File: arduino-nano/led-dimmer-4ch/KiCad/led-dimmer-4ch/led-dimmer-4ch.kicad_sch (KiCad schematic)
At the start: 32 parts, among them J1 Screw_Terminal_01x02, J2 Screw_Terminal_01x08, U1 LM2596S-5

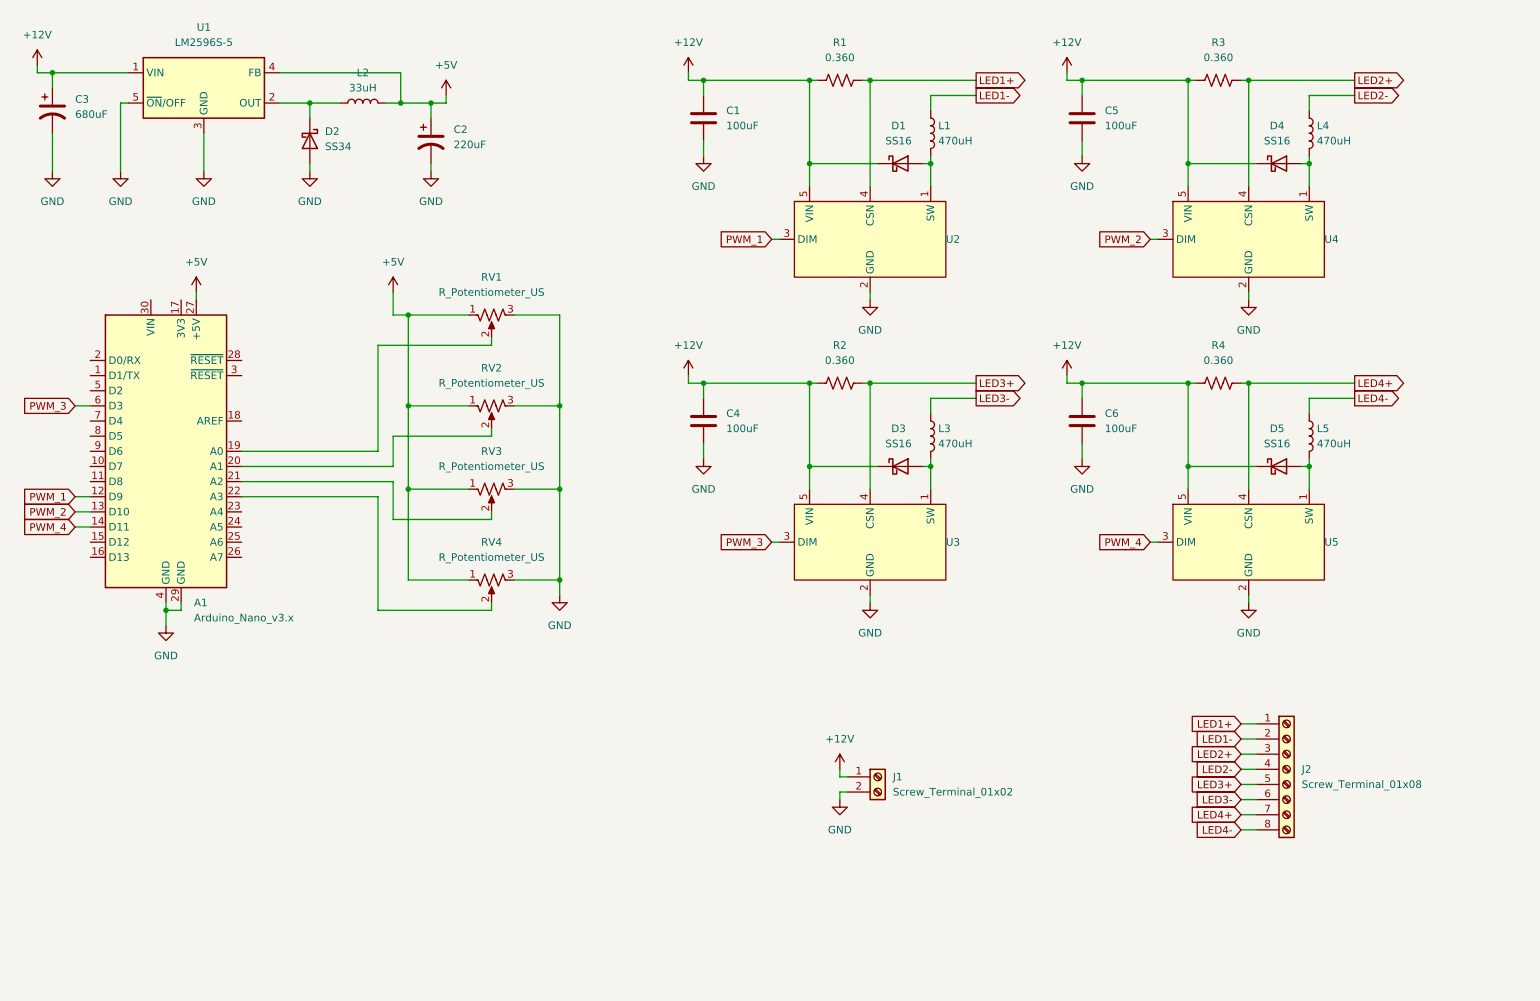
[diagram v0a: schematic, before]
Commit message: feat(led-dimmer-4ch): move pots off-board, swap to the AP63205 buck, and lay out the board
- What: RV1-RV4 become J4/J5 terminals with 100nF ADC caps, LED outputs split across J2/J3, DIM pins get 10k pull-downs, the LM2596 block becomes the microwave's AP63205 layout, and the PCB is placed with identical channel blocks, corner M3 holes, and GND/+12V pours.
- Why: pots now live on a separate panel board, DIM floated high through the PT4115's internal pull-up at reset, the inductors and input caps were outside the datasheet's ranges, and the layout had no outline.
- How: 4-pin 5.00 mm terminals, one 25 mil grid channel template repeated at 500 mil pitch, and the buck block copied from the microwave with nets remapped pad by pad and mirrored to F.Cu.
- Benefit: LEDs stay off through reset, the buck is shared and proven across both boards, and the board shrinks to 3.1 x 2.6 in with USB on the edge.
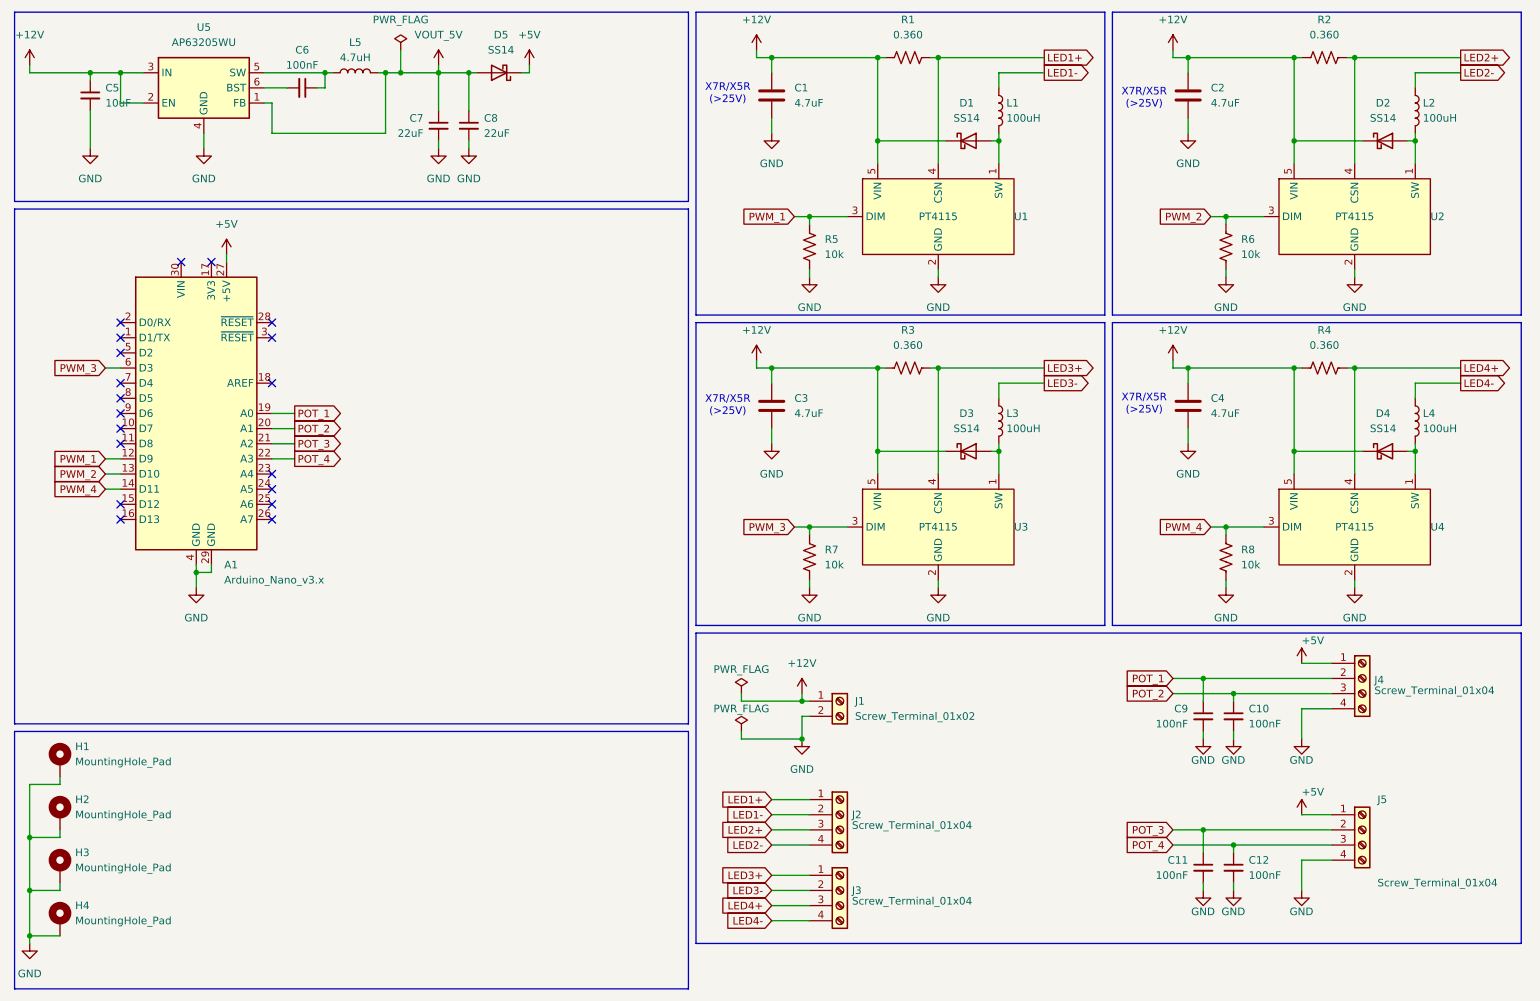
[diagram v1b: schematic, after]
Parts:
- removed C2: 220uF, symbol Device:C_Polarized_US
- removed C3: 680uF, symbol Device:C_Polarized_US
- removed D1, D3, D4, D5: SS16, Diode_SMD:D_SMA, symbol Diode:SS16
- removed D2: SS34, Diode_SMD:D_SMA, symbol Diode:SS34
- removed J2: Screw_Terminal_01x08, symbol Connector:Screw_Terminal_01x08
- removed L2: 33uH, symbol Device:L
- removed R3: 0.360, symbol Device:R_US
- removed RV1, RV2, RV3, RV4: R_Potentiometer_US, symbol Device:R_Potentiometer_US
- removed U1: LM2596S-5, Package_TO_SOT_SMD:TO-263-5_TabPin3, symbol Regulator_Switching:LM2596S-5
- added C10, C11, C12, C6, C9: 100nF, Capacitor_SMD:C_0805_2012Metric_Pad1.18x1.45mm_HandSolder, symbol Device:C_Small
- added C5: 10uF, Capacitor_SMD:C_1210_3225Metric_Pad1.33x2.70mm_HandSolder, symbol Device:C_Small
- added C7, C8: 22uF, Capacitor_SMD:C_1210_3225Metric_Pad1.33x2.70mm_HandSolder, symbol Device:C_Small
- added D1, D2, D3, D4, D5: SS14, Diode_SMD:D_SMA, symbol Diode:SS14
- added H1, H2, H3, H4: MountingHole_Pad, MountingHole:MountingHole_3.2mm_M3_Pad_Via, symbol Mechanical:MountingHole_Pad
- added J2, J3, J4, J5: Screw_Terminal_01x04, TerminalBlock:TerminalBlock_MaiXu_MX126-5.0-04P_1x04_P5.00mm, symbol Connector:Screw_Terminal_01x04
- added L5: 4.7uH, Inductor_SMD:L_Murata_LQH55DN_5.7x5.0mm, symbol Device:L
- added R2: 0.360, Resistor_SMD:R_0805_2012Metric_Pad1.20x1.40mm_HandSolder, symbol Device:R_US
- added R5, R6, R7, R8: 10k, Resistor_SMD:R_0805_2012Metric_Pad1.20x1.40mm_HandSolder, symbol Device:R_US
- added U5: AP63205WU, Package_TO_SOT_SMD:TSOT-23-6, symbol Regulator_Switching:AP63205WU
- C1: value 100uF -> 4.7uF; footprint Capacitor_SMD:C_0805_2012Metric_Pad1.18x1.45mm_HandSolder -> Capacitor_SMD:C_1210_3225Metric_Pad1.33x2.70mm_HandSolder
- C2: renamed from C5; value 100uF -> 4.7uF; footprint Capacitor_SMD:C_0805_2012Metric_Pad1.18x1.45mm_HandSolder -> Capacitor_SMD:C_1210_3225Metric_Pad1.33x2.70mm_HandSolder
- C3: renamed from C4; value 100uF -> 4.7uF; footprint Capacitor_SMD:C_0805_2012Metric_Pad1.18x1.45mm_HandSolder -> Capacitor_SMD:C_1210_3225Metric_Pad1.33x2.70mm_HandSolder
- C4: renamed from C6; value 100uF -> 4.7uF; footprint Capacitor_SMD:C_0805_2012Metric_Pad1.18x1.45mm_HandSolder -> Capacitor_SMD:C_1210_3225Metric_Pad1.33x2.70mm_HandSolder
- J1: footprint (none) -> TerminalBlock_MetzConnect:TerminalBlock_MetzConnect_Type011_RT05502HBLC_1x02_P5.00mm_Horizontal
- L1, L3: value 470uH -> 100uH; footprint (none) -> Inductor_SMD:L_Coilcraft_MSS1038-XXX
- L2: renamed from L4; value 470uH -> 100uH; footprint (none) -> Inductor_SMD:L_Coilcraft_MSS1038-XXX
- L4: renamed from L5; value 470uH -> 100uH; footprint (none) -> Inductor_SMD:L_Coilcraft_MSS1038-XXX
- U1: renamed from U2; value (none) -> PT4115
- U2: renamed from U4; value (none) -> PT4115
- U3: value (none) -> PT4115
- U4: renamed from U5; value (none) -> PT4115
- renumbered R2 to R3
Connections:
- net +12V: now also C5.1, D1.1 (K), D2.1 (K), D3.1 (K), D4.1 (K), R2.1, U5.2 (EN), U5.3 (IN)
- net +5V: now also D5.1 (K), J4.1 (Pin_1), J5.1 (Pin_1)
- net GND: now also C10.2, C11.2, C12.2, C5.2, C7.2, C8.2, C9.2, H1.1, H2.1, H3.1, H4.1, J4.4 (Pin_4), J5.4 (Pin_4), R5.2, R6.2, R7.2, R8.2, U5.4 (GND)
- net LED1+: now also J2.1 (Pin_1)
- net LED1-: now also J2.2 (Pin_2)
- net LED2+: now also J2.3 (Pin_3), R2.2
- net LED2-: now also J2.4 (Pin_4)
- net LED3+: now also J3.1 (Pin_1)
- net LED3-: now also J3.2 (Pin_2)
- net LED4+: now also J3.3 (Pin_3)
- net LED4-: now also J3.4 (Pin_4)
- net PWM_1: now also R5.1
- net PWM_2: now also R6.1
- net PWM_3: now also R7.1
- net PWM_4: now also R8.1
- net POT_2: now reaches A1.20 (A1)
- net POT_2: now also C10.1, J4.3 (Pin_3)
- net at L3.2, U3.1 (SW): now also D3.2 (A)
- net POT_1: now reaches A1.19 (A0)
- net POT_1: now also C9.1, J4.2 (Pin_2)
- net POT_3: now reaches A1.21 (A2)
- net POT_3: now also C11.1, J5.2 (Pin_2)
- net POT_4: now reaches A1.22 (A3)
- net POT_4: now also C12.1, J5.3 (Pin_3)
- net at L1.2, U1.1 (SW): now also D1.2 (A)
- net at L4.2, U4.1 (SW): now also D4.2 (A)
- net at L2.2, U2.1 (SW): now also D2.2 (A)
- new net: C6.1, L5.1, U5.5 (SW)
- new net: C6.2, U5.6 (BST)
- new net VOUT_5V: C7.1, C8.1, D5.2 (A), L5.2, U5.1 (FB)
- no-connect marks 0 -> 19
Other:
- note added: "X7R/X5R (>25V)"
- moved on the sheet: A1, C1, C2, C3, C4, J1, L1, L2, L3, L4, R1, R3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

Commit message: refactor(led-dimmer-4ch): move terminals to Phoenix MKDS 5.08 mm and snap placement to the 25 mil grid
- What: swaps J1 to TerminalBlock_Phoenix_MKDS-1,5-2-5.08 and J2-J5 to TerminalBlock_Phoenix_MKDS-1,5-4-5.08 in the schematic and PCB, rotates the terminals to face the board edges, moves the Nano down, and snaps J1 and A1 onto the 25 mil grid.
- Why: the MaiXu and Metz 5.00 mm footprints put every pad after pin 1 off the mil grid, and the microwave already uses MKDS 5.08 mm.
- How: replaced each footprint in place keeping pin 1, nets, fields, and label positions, then refilled zones.
- Benefit: every terminal pad sits 200 mil apart on the board grid, and both boards order the same terminal part.
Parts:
- J1: footprint TerminalBlock_MetzConnect:TerminalBlock_MetzConnect_Type011_RT05502HBLC_1x02_P5.00mm_Horizontal -> TerminalBlock_Phoenix:TerminalBlock_Phoenix_MKDS-1,5-2-5.08_1x02_P5.08mm_Horizontal
- J2, J3, J4, J5: footprint TerminalBlock:TerminalBlock_MaiXu_MX126-5.0-04P_1x04_P5.00mm -> TerminalBlock_Phoenix:TerminalBlock_Phoenix_MKDS-1,5-4-5.08_1x04_P5.08mm_Horizontal
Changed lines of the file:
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@@
 			)
 		)
-		(property "Footprint" "TerminalBlock:TerminalBlock_MaiXu_MX126-5.0-04P_1x04_P5.00mm"
+		(property "Footprint" "TerminalBlock_Phoenix:TerminalBlock_Phoenix_MKDS-1,5-4-5.08_1x04_P5.08mm_Horizontal"
 			(at 152.4 161.29 0)
 			(hide yes)
@@
 			)
 		)
-		(property "Footprint" "TerminalBlock:TerminalBlock_MaiXu_MX126-5.0-04P_1x04_P5.00mm"
+		(property "Footprint" "TerminalBlock_Phoenix:TerminalBlock_Phoenix_MKDS-1,5-4-5.08_1x04_P5.08mm_Horizontal"
 			(at 240.03 151.13 0)
 			(hide yes)
@@
 			)
 		)
-		(property "Footprint" "TerminalBlock_MetzConnect:TerminalBlock_MetzConnect_Type011_RT05502HBLC_1x02_P5.00mm_Horizontal"
+		(property "Footprint" "TerminalBlock_Phoenix:TerminalBlock_Phoenix_MKDS-1,5-2-5.08_1x02_P5.08mm_Horizontal"
 			(at 152.4 129.54 0)
 			(hide yes)
@@
 			)
 		)
-		(property "Footprint" "TerminalBlock:TerminalBlock_MaiXu_MX126-5.0-04P_1x04_P5.00mm"
+		(property "Footprint" "TerminalBlock_Phoenix:TerminalBlock_Phoenix_MKDS-1,5-4-5.08_1x04_P5.08mm_Horizontal"
 			(at 152.4 148.59 0)
 			(hide yes)
@@
 			)
 		)
-		(property "Footprint" "TerminalBlock:TerminalBlock_MaiXu_MX126-5.0-04P_1x04_P5.00mm"
+		(property "Footprint" "TerminalBlock_Phoenix:TerminalBlock_Phoenix_MKDS-1,5-4-5.08_1x04_P5.08mm_Horizontal"
 			(at 240.03 125.73 0)
 			(hide yes)

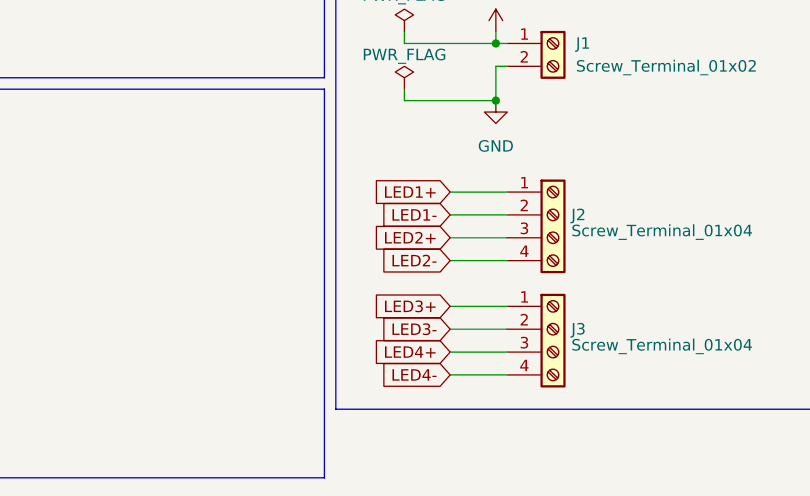
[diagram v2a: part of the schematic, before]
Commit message: feat(led-dimmer-4ch): route the board on the mil standard with solid pours
- What: routes every net on 2 layers, reverses the J2/J3 net labels so pins 4 to 1 carry LED1+, LED1-, LED2+, LED2- (J3 the same for channels 3 and 4), adds Default (10 mil) and Power (20 mil) net classes, and sets all pours to solid pad connections.
- Why: the board had 39 unconnected pads, and rotating J2/J3 outward reversed their pin order against the driver order, so every LED pair would have crossed.
- How: SW, LED, and pot nets on F.Cu, PWM and +5V on B.Cu under the +12V strip, GND stitching vias at each PT4115 tab, inductor, filter cap, and enclosed pocket, with all tracks at 10, 20, or 60 mil and every via 24/12 mil.
- Benefit: DRC reports 0 violations and 0 unconnected pads, ERC is clean, and the firmware pin map (D9, D10, D3, D11 and A0 to A3) is unchanged.
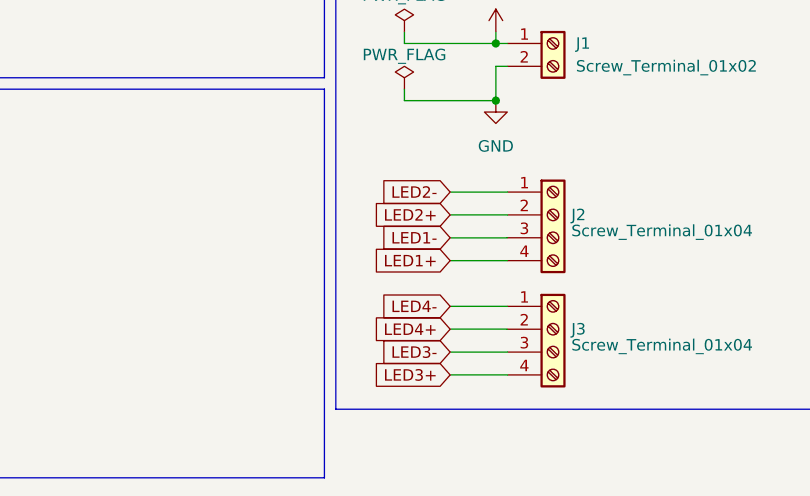
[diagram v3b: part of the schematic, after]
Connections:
- net LED1+: now also J2.4 (Pin_4); no longer J2.1 (Pin_1)
- net LED1-: now also J2.3 (Pin_3); no longer J2.2 (Pin_2)
- net LED2+: now also J2.2 (Pin_2); no longer J2.3 (Pin_3)
- net LED2-: now also J2.1 (Pin_1); no longer J2.4 (Pin_4)
- net LED3+: now also J3.4 (Pin_4); no longer J3.1 (Pin_1)
- net LED3-: now also J3.3 (Pin_3); no longer J3.2 (Pin_2)
- net LED4+: now also J3.2 (Pin_2); no longer J3.3 (Pin_3)
- net LED4-: now also J3.1 (Pin_1); no longer J3.4 (Pin_4)
